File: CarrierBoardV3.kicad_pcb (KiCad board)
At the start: 4 copper layers, 92 x 96 mm, 91 parts, among them J1 USB_B_Micro, J10 Conn_02x26_Odd_Even, J11 SW1-12V_SHUNT, J12 SW8-3V3_SHUNT, J13 SW5-5V_SHUNT, J2 Conn_02x09_Odd_Even, J3 Barrel_Jack, J4 TX2iConnctor, J5 Conn_01x03_Male, J6 Conn_02x04_Odd_Even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

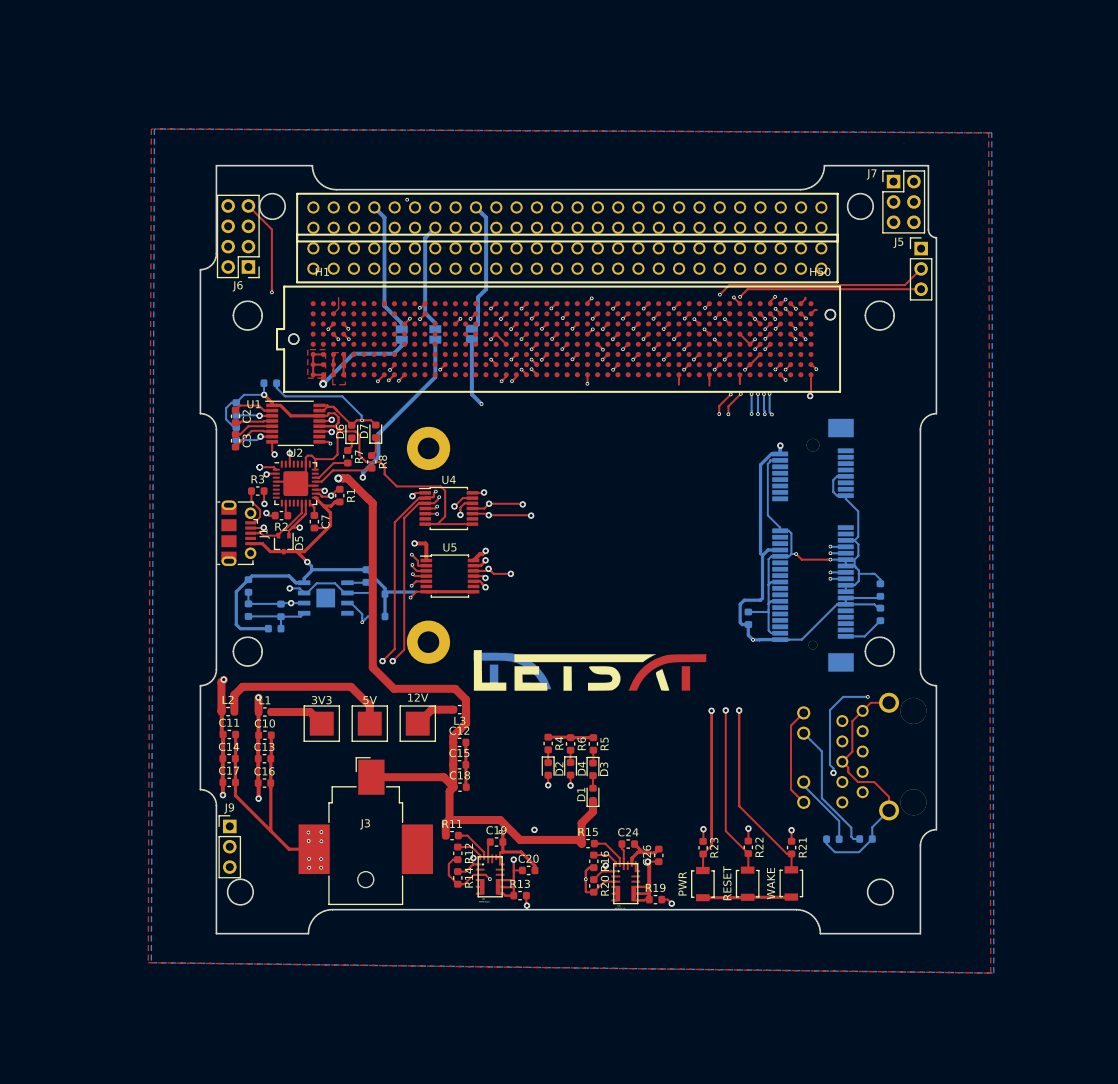
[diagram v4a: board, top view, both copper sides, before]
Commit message: Routed all new edits done to PC104
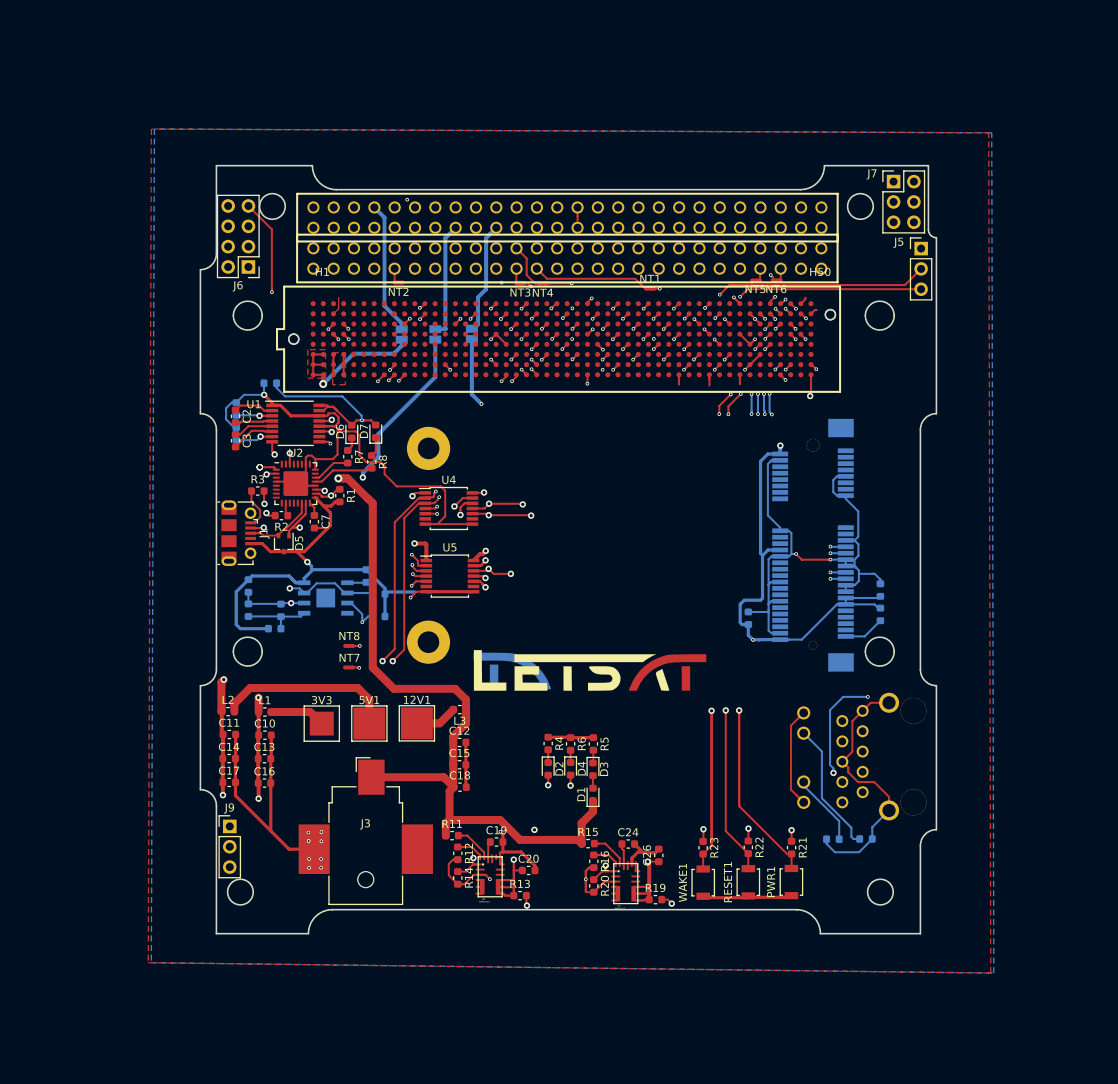
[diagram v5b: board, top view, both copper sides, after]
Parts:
- removed 12V: 12V, TestPoint:TestPoint_Pad_4.0x4.0mm
- removed 5V: 5V, TestPoint:TestPoint_Pad_4.0x4.0mm
- removed PWR, RESET, WAKE: SW_Push, Button_Switch_SMD:SW_SPST_B3U-1000P
- added 12V1: 12V, TestPoint:TestPoint_Pad_4.0x4.0mm, F.Cu at (127.3, 112.8)
- added 5V1: 5V, TestPoint:TestPoint_Pad_4.0x4.0mm, F.Cu at (121.4, 112.8)
- added NT1: SPI_MOSI, NetTie:NetTie-2_SMD_Pad0.5mm, F.Cu at (156.5, 58.4)
- added NT2: SPI_A, NetTie:NetTie-2_SMD_Pad0.5mm, F.Cu at (125.0, 57.7)
- added NT3: SPI_CLK, NetTie:NetTie-2_SMD_Pad0.5mm, F.Cu at (140.2, 57.7)
- added NT4: SPI_MISO, NetTie:NetTie-2_SMD_Pad0.5mm, F.Cu at (143.0, 57.8)
- added NT5: SDA_B, NetTie:NetTie-2_SMD_Pad0.5mm, F.Cu at (169.7, 57.4)
- added NT6: SCL_B, NetTie:NetTie-2_SMD_Pad0.5mm, F.Cu at (172.3, 57.4)
- added NT7: UART_TXJETSON, NetTie:NetTie-2_SMD_Pad0.5mm, F.Cu at (118.8, 105.8)
- added NT8: UART_RXJETSON, NetTie:NetTie-2_SMD_Pad0.5mm, F.Cu at (118.8, 103.1)
- added PWR1: SW_Push, Button_Switch_SMD:SW_SPST_B3U-1000P, F.Cu at (174.1, 132.6)
- added RESET1: SW_Push, Button_Switch_SMD:SW_SPST_B3U-1000P, F.Cu at (168.7, 132.6)
- added WAKE1: SW_Push, Button_Switch_SMD:SW_SPST_B3U-1000P, F.Cu at (163.1, 132.7)
- J12: value SW8-3V3_SHUNT -> SW9-3V3_SHUNT
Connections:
- net Net-(J10-Pad49) renamed DTMF1
- net Net-(J10-Pad50) renamed DTMF2
- net Net-(J10-Pad51) renamed DTMF3
- net Net-(J10-Pad52) renamed DTMF4
- net Net-(J8-Pad1) renamed GPIO_A
- net Net-(J8-Pad10) renamed SPI_CS_B
- net Net-(J8-Pad11) renamed SPI_CS_C
- net Net-(J8-Pad12) renamed SPI_CS_D
- net Net-(J8-Pad13) renamed SPI_CS_E
- net Net-(J8-Pad14) renamed SPI_CS_F
- net Net-(J8-Pad15) renamed GPIO_J
- net Net-(J8-Pad16) renamed GPIO_K
- net Net-(J8-Pad17) renamed GPIO_L
- net Net-(J8-Pad18) renamed GPIO_M
- net Net-(J8-Pad2) renamed GPIO_B
- net Net-(J8-Pad24) renamed SPI_CS
- net Net-(J8-Pad27) renamed GPIO_R
- net Net-(J8-Pad28) renamed GPIO_S
- net Net-(J8-Pad29) renamed GPIO_T
- net Net-(J8-Pad3) renamed GPIO_C
- net Net-(J8-Pad30) renamed GPIO_U
- net Net-(J8-Pad31) renamed GPIO_V
- net Net-(J8-Pad34) renamed UART_B_RX_LVTTL_GPS
- net Net-(J8-Pad36) renamed UART_B_TX_LVTTL_GPS
- net Net-(J8-Pad37) renamed UART_C_RS485+
- net Net-(J8-Pad38) renamed UART_E_RS485+
- net Net-(J8-Pad39) renamed UART_C_RS485-
- net Net-(J8-Pad4) renamed GPIO_D
- net Net-(J8-Pad40) renamed UART_E_RS485-
- net Net-(J8-Pad42) renamed CAN_H
- net Net-(J8-Pad44) renamed CAN_L
- net Net-(J8-Pad5) renamed GPIO_E
- net Net-(J8-Pad6) renamed GPIO_F
- net Net-(J8-Pad7) renamed GPIO_G
- net Net-(J8-Pad8) renamed GPIO_H
- net TX2i_VBATT renamed VBATT
- J10 pad 27: Net-(J10-Pad27) -> 3V3_PLAT
- J10 pad 28: Net-(J10-Pad28) -> 3V3_PLAT
- J12 pad 1: SW8 -> SW9
- J13 pad 1: SW5 -> SW6
- J8 pad 21: Net-(J8-Pad21) -> SPI_CLK
- J8 pad 22: Net-(J8-Pad22) -> SPI_MISO
- J8 pad 23: Net-(J8-Pad23) -> SPI_MOSI
- J8 pad 41: I2C_GP1_DAT -> SDA_A
- J8 pad 43: I2C_GP1_CK -> SCL_A
- J8 pad 45: Net-(J8-Pad45) -> SDA_B
- J8 pad 47: Net-(J8-Pad47) -> SCL_B
- J8 pad 9: Net-(J8-Pad9) -> SPI_CS_A
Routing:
- net SPI0_CS0#: track 90.4 -> 122.8 mm, vias 1 -> 3
- net Net-(L2-Pad2): track 22.6 -> 0.00 mm
- net Net-(5V1-Pad1): track 0.00 -> 22.3 mm
- net SW8: track 16.5 -> 0.00 mm
- net SPI_MOSI: track 0.00 -> 14.7 mm
- net SW6: track 0.00 -> 14.5 mm
- net SW9: track 0.00 -> 14.0 mm
- net SW5: track 13.7 -> 0.00 mm
- net SPI0_CLK: track 90.7 -> 101.6 mm, vias 1 -> 3
- net SPI0_MOSI: track 90.3 -> 98.5 mm, vias 2 -> 4
- net SPI0_MISO: track 93.1 -> 100.2 mm, vias 1 -> 3
- net SPI_MISO: track 0.00 -> 5.80 mm
- net I2C_GP1_CK: track 89.2 -> 94.9 mm, vias 3 -> 4
- net UART0_TX: track 90.5 -> 96.1 mm, vias 3 -> 4
- net Net-(12V1-Pad1): track 0.00 -> 5.28 mm
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
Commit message: Finished Ready for FAB
S/N:0C137_V3_SP19
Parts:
- added REF**: ESD-Logo_6.6x6mm_SilkScreen, Symbol:ESD-Logo_6.6x6mm_SilkScreen, B.Cu at (127.1, 118.5)
- added REF**: WEEE-Logo_4.2x6mm_SilkScreen, Symbol:WEEE-Logo_4.2x6mm_SilkScreen, B.Cu at (116.2, 118.7)
- added REF**: ESD-Logo_6.6x6mm_SilkScreen, Symbol:ESD-Logo_6.6x6mm_SilkScreen, F.Cu at (166.0, 120.8)
- moved NT7 61.4 mm to (157.2, 57.8), turned to 90 degrees
- moved NT8 60.1 mm to (158.4, 57.8), turned to 270 degrees
- moved NT1 1.04 mm to (155.6, 57.8)
- moved NT5 0.55 mm to (170.2, 57.3), turned to 90 degrees
- renumbered 12V1 to 12V, 5V1 to 5V, PWR1 to PWR, RESET1 to RESET, WAKE1 to WAKE
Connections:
- J3 pad 3: (no net) -> GBE_CTREF(GND)
- J8 pad 33: Net-(J8-Pad33) -> UART_A_RX_LVTTL
- J8 pad 35: Net-(J8-Pad35) -> UART_A_TX_LVTTL
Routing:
- net UART0_RX: track 95.0 -> 123.8 mm
- net TX2i_3V3: track 381.7 -> 353.7 mm
- net UART0_TX: track 96.1 -> 120.5 mm, vias 4 -> 3
- net GBE_MDI2-: track 87.1 -> 68.9 mm
- net SATA_RX+: track 55.5 -> 42.1 mm, vias 4 -> 3
- net SATA_RX-: track 52.3 -> 40.3 mm, vias 4 -> 3
- net I2C_GP1_DAT: track 85.8 -> 82.6 mm
- net UART_A_RX_LVTTL: track 0.00 -> 2.82 mm
- net I2C_GP1_CK: track 94.9 -> 93.1 mm
- net UART_A_TX_LVTTL: track 0.00 -> 1.71 mm
- net GBE_CTREF(GND): track 419.1 -> 420.2 mm, vias 78 -> 79
- net SPI_MOSI: track 14.7 -> 13.6 mm
- net SPI0_CS0#: track 122.8 -> 122.2 mm
- net SDA_B: track 1.50 -> 0.98 mm
- net SATA_TX-: track 41.6 -> 41.1 mm, vias 4 -> 3
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- added copper zone on F.Cu, net TX2i_3V3
- added copper zone on F.Cu, net TX2i_5V
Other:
- net class Default: trace_width 0.25 -> 0.254
- board text added: "+"
- board text added: "-"
- board text added: "GROUND UNIT DO NOT FLY"
- board text added: "Prabodh Jhaveri Daniel Lopez"
- board text added: "S/N: 0C137_V3_SP19"
- board text added: "SW6_SHUNT5V"
- board text added: "SW9_SHUNT3V3"
- board text removed: "SW5_SHUNT5V"
- board text removed: "SW8_SHUNT3V3"

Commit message: minor changes
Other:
- board text added: "Model: 0C137_V3_SP19"
- board text added: "S/N:"
- board text removed: "S/N: 0C137_V3_SP19"
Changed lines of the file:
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@@
   (general
     (thickness 1.6)
-    (drawings 63)
+    (drawings 67)
     (tracks 5298)
     (zones 0)
@@
   )
   (setup
-    (last_trace_width 0.4)
+    (last_trace_width 0.254)
     (user_trace_width 0.1)
     (user_trace_width 0.15)
@@
       (xy -1.677906 0.291158)) (layer F.SilkS) (width 0.01))
   )
+  (gr_poly (pts (xy 173.355 125.222) (xy 173.355 121.539) (xy 174.498 121.539) (xy 174.498 125.222)) (layer B.SilkS) (width 0.15))
+  (gr_poly (pts (xy 169.418 124.079) (xy 173.355 124.079) (xy 173.355 125.222) (xy 169.418 125.222)) (layer B.SilkS) (width 0.15))
+  (gr_poly (pts (xy 169.418 121.539) (xy 173.355 121.539) (xy 173.355 122.682) (xy 169.418 122.682)) (layer B.SilkS) (width 0.15))
+  (gr_text S/N: (at 171.323 123.317) (layer B.Mask)
+    (effects (font (size 0.7 0.7) (thickness 0.175)) (justify mirror))
+  )
   (gr_text "GROUND UNIT\nDO NOT FLY" (at 148.082 100.203) (layer F.Mask)
     (effects (font (size 1.5 1.5) (thickness 0.3)))
@@
   )
   (gr_circle (center 109.395113 125.408387) (end 109.395113 124.408387) (layer F.SilkS) (width 0.2))
-  (gr_poly (pts (xy 153.67 121.539) (xy 153.67 125.222) (xy 173.228 125.222) (xy 173.228 121.539) (xy 167.513 121.539)) (layer B.SilkS) (width 0.15))
+  (gr_poly (pts (xy 149.86 121.539) (xy 149.86 125.222) (xy 169.418 125.222) (xy 169.418 121.539) (xy 163.703 121.539)) (layer B.SilkS) (width 0.15))
   (gr_text "GROUND UNIT\nDO NOT FLY" (at 149.098 113.919) (layer B.Mask)
     (effects (font (size 1.5 1.5) (thickness 0.3)) (justify mirror))
   )
-  (gr_text "S/N: 0C137_V3_SP19" (at 170.307 132.08) (layer B.Mask)
+  (gr_text "Model: 0C137_V3_SP19" (at 170.307 132.08) (layer B.Mask)
     (effects (font (size 0.5 0.5) (thickness 0.125)) (justify mirror))
   )
@@
   (gr_arc (start 106.1632 103.7862) (end 104.3632 103.7862) (angle -180) (layer Edge.Cuts) (width 0.2))
   (gr_arc (start 185.1632 61.7862) (end 183.3632 61.7862) (angle -180) (layer Edge.Cuts) (width 0.2))
-  (via (at 158.369 58.293) (size 0.457) (drill 0.254) (layers F.Cu B.Cu) (net 234))
   (via (at 139.4132 129.7862) (size 0.8) (drill 0.4) (layers F.Cu B.Cu) (net 1))
   (segment (start 138.338201 134.2862) (end 138.088201 134.0362) (width 0.25) (layer F.Cu) (net 1))
@@
   (segment (start 126.422853 92.9386) (end 126.288793 92.80454) (width 0.254) (layer In2.Cu) (net 202))
   (segment (start 126.746 92.9386) (end 126.422853 92.9386) (width 0.254) (layer In2.Cu) (net 202))
+  (via (at 158.369 58.293) (size 0.457) (drill 0.254) (layers F.Cu B.Cu) (net 234))
   (via (at 129.6682 83.7762) (size 0.457) (drill 0.254) (layers F.Cu B.Cu) (net 234))
   (via (at 123.0122 104.9782) (size 0.8) (drill 0.4) (layers F.Cu B.Cu) (net 234))

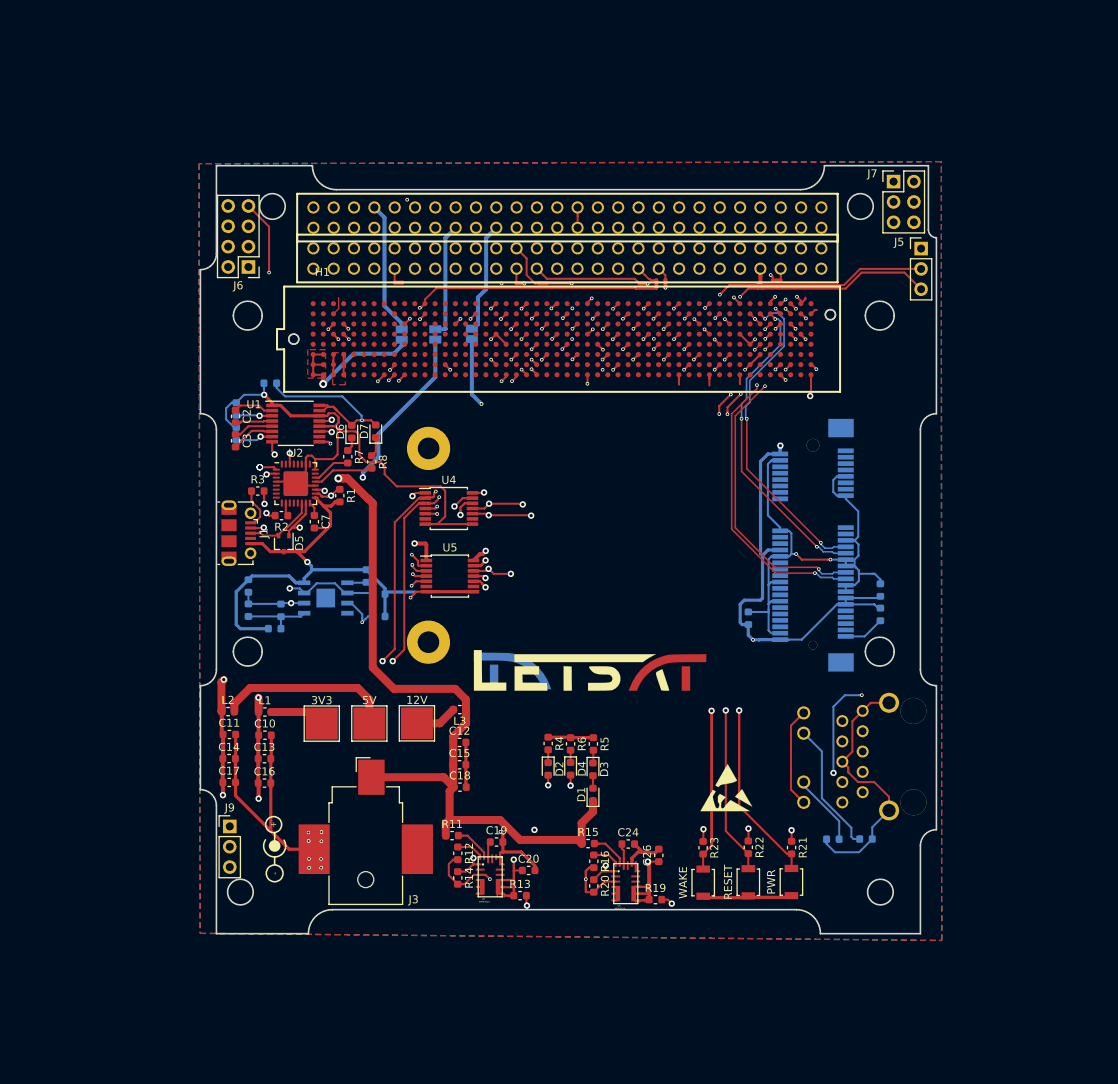
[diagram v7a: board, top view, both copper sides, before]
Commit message: Fixed TX2i connector orientation, all traces done, trace matching needs to be done still
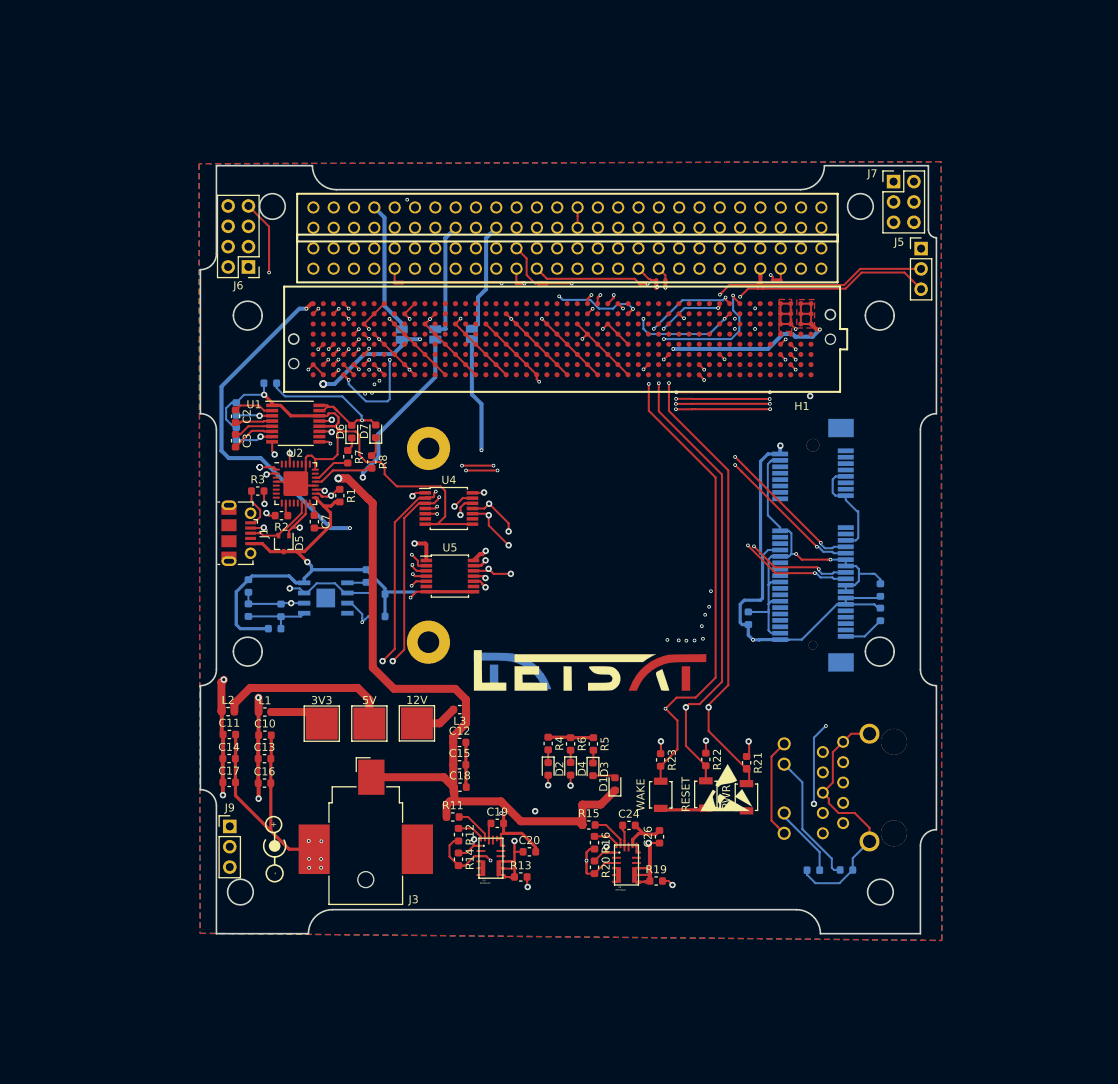
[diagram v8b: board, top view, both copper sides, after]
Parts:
- moved R22 12.2 mm to (163.4, 117.3)
- moved R23 12.2 mm to (157.8, 117.3)
- moved RESET 12.2 mm to (163.4, 121.6)
- moved WAKE 12.2 mm to (157.8, 121.7)
- moved R21 12.0 mm to (168.5, 117.7)
- moved PWR 12.0 mm to (168.5, 122.0)
- moved J2 4.57 mm to (197.7, 120.9)
- moved R9 4.57 mm to (176.9, 131.1)
- moved R10 4.57 mm to (181.0, 131.1)
- moved D1 3.04 mm to (152.1, 120.3)
- moved R12 2.33 mm to (132.5, 126.7)
- moved R14 2.33 mm to (132.5, 129.7)
- moved R16 2.33 mm to (149.5, 127.7)
- moved R19 2.33 mm to (157.2, 132.5)
- moved R20 2.33 mm to (149.5, 130.7)
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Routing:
- net TX2i_12V: track 127.1 -> 182.9 mm, vias 2 -> 5
- net SPI0_CS: track 40.4 -> 87.9 mm, vias 2 -> 4
- net SPI0_MI: track 35.5 -> 81.6 mm, vias 2 -> 4
- net GPO0: track 28.5 -> 74.3 mm, vias 1 -> 2
- net SPI0_CK: track 36.8 -> 81.6 mm, vias 2 -> 4
- net TX2i_3V3: track 353.7 -> 396.9 mm, vias 9 -> 11
- net SATA_TX-: track 41.1 -> 83.5 mm
- net I2C_CK: track 23.0 -> 63.2 mm
- net SPI0_MO: track 39.4 -> 79.4 mm, vias 2 -> 4
- net SATA_TX+: track 41.8 -> 81.7 mm
- net GPI3: track 33.4 -> 73.2 mm, vias 2 -> 3
- net GPO1: track 32.9 -> 71.1 mm, vias 1 -> 2
- net GBE_MDI3+: track 87.1 -> 123.3 mm, vias 1 -> 3
- net GBE_CTREF(GND): track 420.2 -> 455.3 mm, vias 79 -> 36
- net GPI0: track 30.0 -> 65.1 mm, vias 1 -> 2
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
